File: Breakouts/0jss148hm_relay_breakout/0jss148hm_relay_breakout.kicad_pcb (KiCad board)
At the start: 2 copper layers, 40 x 11 mm, 13 parts, among them J1 Conn_01x03, J2 Conn_01x01, J4 Conn_01x01, J5 Conn_01x02, K1 G5Q-1A, Q1 Q_PNP_BEC, U1 PC817

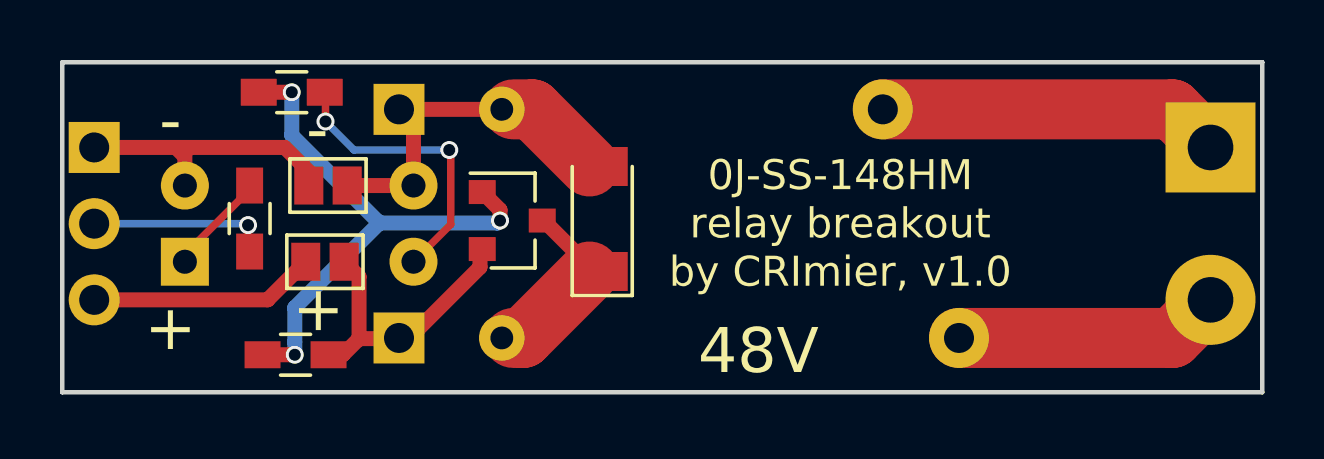
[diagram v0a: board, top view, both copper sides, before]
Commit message: Updating and renaming a 48V relay breakout PCB, sch is broken and no idea how to fix it, really - maybe eventually. Also adding a 2x9 panel that fits inside JLCPCB 10x10 dimensions, though will take extra money to be produced because the PCBs are too narrow.
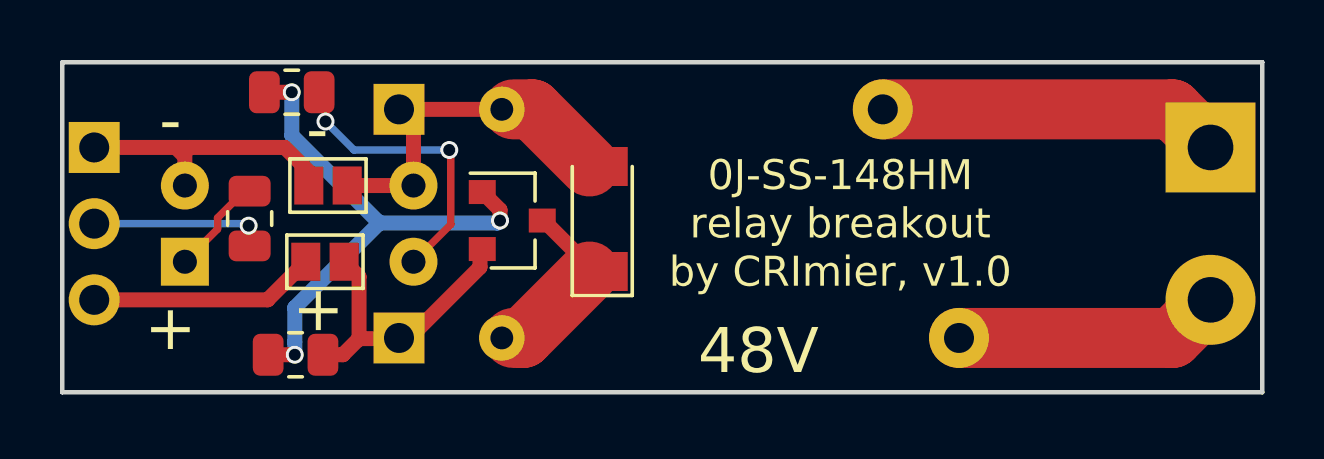
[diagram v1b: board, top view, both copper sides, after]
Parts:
- R1, R2, R3: footprint Resistors_SMD:R_0603_HandSoldering -> Resistor_SMD:R_0805_2012Metric

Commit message: Adding a README and changing the on-PCB text to say "v2" because that's what it is. Need to also update the panel text sometime soon.
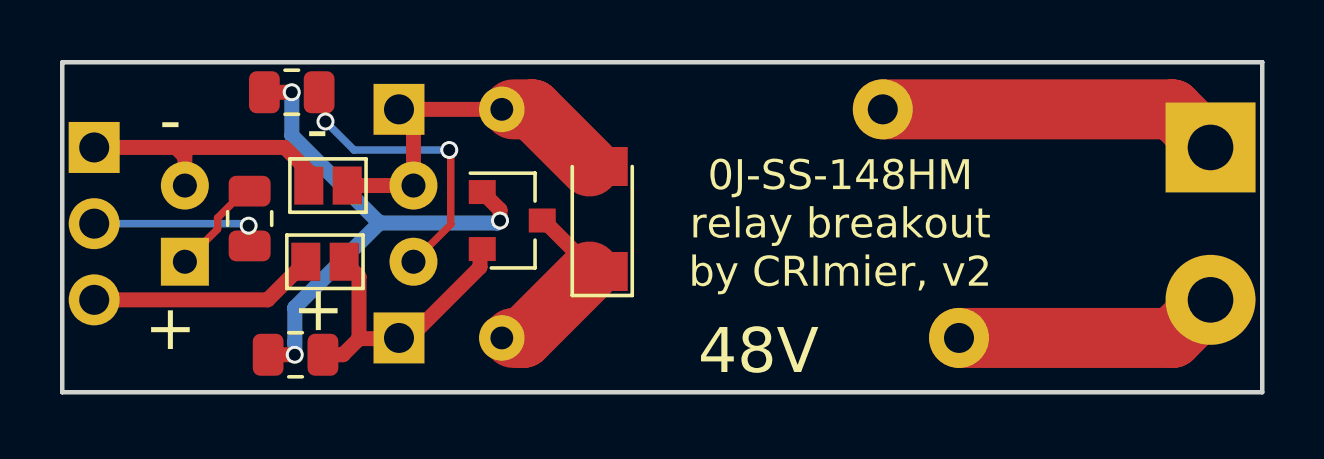
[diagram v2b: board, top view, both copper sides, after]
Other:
- board text added: "0J-SS-148HM relay breakout by CRImier, v2"
- board text removed: "0J-SS-148HM relay breakout by CRImier, v1.0"
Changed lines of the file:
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@@
     (effects (font (size 1.5 1.5) (thickness 0.3)))
   )
-  (gr_text "0J-SS-148HM\nrelay breakout\nby CRImier, v1.0" (at 150.433 109.577) (layer F.SilkS)
+  (gr_text "0J-SS-148HM\nrelay breakout\nby CRImier, v2" (at 150.433 109.577) (layer F.SilkS)
     (effects (font (size 1 1) (thickness 0.2)))
   )
